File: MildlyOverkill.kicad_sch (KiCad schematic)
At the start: 68 parts, among them J1 USB_C_Receptacle_USB2.0_16P, J2 2604-1102, J3 2604-1104, J4 2604-1104, J5 Conn_01x04_Pin, J6 Conn_01x04_MountingPin, J7 Conn_01x04_Pin, Q5 QM6015D, U1 ESP32-S3-WROOM-1, U2 MCP3208, U3 LD1117S33TR_SOT223, U5 USBLC6-2P6, U6 TPS62932

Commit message: Added ethernet and ntcs
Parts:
- removed D24: 5V, LED_SMD:LED_0603_1608Metric, symbol Device:LED
- added C21, C36, C37, C38, C39, C40, C41: 0.1uF, symbol Device:C
- added C26, C35: 10uF 16V, symbol Device:C_Polarized
- added C27: 4.7uF, symbol Device:C
- added C28, C29, C30, C31: 10nF, symbol Device:C
- added C32: 22nF, symbol Device:C
- added C33, C34: 18pF, symbol Device:C
- added C42: 1nF 10kV, symbol Device:C
- added FB2: GZ2012D121TF, Inductor_THT:Choke_Schaffner_RN102-04-14.0x14.0mm, symbol Device:FerriteBead
- added J8: RJ45_Wuerth_7499010211A, Connector_RJ:RJ45_Wuerth_7499010211A_Horizontal, symbol Connector:RJ45_Wuerth_7499010211A
- added R41: 12.4K, Resistor_SMD:R_0805_2012Metric, symbol Device:R
- added R42, R43: 82, symbol Device:R
- added R44: 49, symbol Device:R
- added R66: 10, symbol Device:R
- added R73: 1M, symbol Device:R
- added R74: 0, symbol Device:R
- added R75, R76: 330, Resistor_SMD:R_0805_2012Metric, symbol Device:R
- added R77, R78, R79: R, symbol Device:R
- added TH1, TH2, TH3: Thermistor_NTC, Resistor_SMD:R_0805_2012Metric_Pad1.20x1.40mm_HandSolder, symbol Device:Thermistor_NTC
- added U7: W5500, Package_QFP:LQFP-48_7x7mm_P0.5mm, symbol Interface_Ethernet:W5500
- added Y1: 3134250001, Crystal:Crystal_SMD_3225-4Pin_3.2x2.5mm_HandSoldering, symbol Device:Crystal_GND24
- R62: value 210 -> 49; footprint Resistor_SMD:R_0805_2012Metric -> (none)
- R64, R65, R67, R68, R69, R70, R71, R72: footprint Resistor_SMD:R_0603_1608Metric_Pad0.98x0.95mm_HandSolder -> Resistor_SMD:R_0805_2012Metric_Pad1.20x1.40mm_HandSolder
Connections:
- net +3.3V: now also C21.1, C26.1, FB2.1, R77.1, R78.1, R79.1, U7.28 (VDD)
- net GND: now also D11.1 (K), D12.1 (K), D13.1 (K), D23.1 (K), C21.2, C26.2, C27.2, C28.2, C29.2, C32.1, C33.2, C34.2, C35.2, C36.2, C37.2, C38.2, C39.2, C40.2, C41.2, C42.1, J8.10, J8.11, R41.2, TH1.2, TH2.2, TH3.2, U7.14 (AGND), U7.16 (AGND), U7.19 (AGND), U7.29 (GND), U7.3 (AGND), U7.48 (AGND), U7.9 (AGND), Y1.2 (G), Y1.4 (G); no longer D11.2 (A), D12.2 (A), D13.2 (A), D23.2 (A)
- net MISO: now also U7.34 (MISO)
- net MOSI: now also U7.35 (MOSI)
- net SCLK: now also U7.33 (SCLK)
- net NTC1: now reaches U2.5 (CH4)
- net NTC1: now also R77.2, TH1.1
- net NTC2: now reaches U2.6 (CH5)
- net NTC2: now also R78.2, TH2.1
- net NTC3: now reaches U2.7 (CH6)
- net NTC3: now also R79.2, TH3.1
- net at R53.2: now also D12.2 (A); no longer D12.1 (K)
- net at R52.2: now also D11.2 (A); no longer D11.1 (K)
- net at R61.2: now also D23.2 (A); no longer D23.1 (K)
- net at R54.2: now also D13.2 (A); no longer D13.1 (K)
- net at R62.2: now also J8.2 (TD-), U7.1 (TXN)
- net LED2 renamed +3.3VA
- net +3.3VA: now also C35.1, C36.1, C37.1, C38.1, C39.1, C40.1, C41.1, FB2.2, R44.1, R66.1, U7.11 (AVDD), U7.15 (AVDD), U7.17 (AVDD), U7.21 (AVDD), U7.4 (AVDD), U7.8 (AVDD); no longer U1.31 (IO38)
- new net: C30.1, R43.1, U7.5 (RXN)
- new net: C30.2, J8.6 (RD-)
- new net: C32.2, J8.4 (CTD), R66.2
- new net: C28.1, U7.22 (1V2O)
- new net: J8.1 (TD+), R44.2, U7.2 (TXP)
- new net: R73.1, R74.2, U7.31 (XO)
- new net: C34.1, R73.2, U7.30 (XI/CLKIN), Y1.3
- new net: J8.9, R76.2
- new net: R41.1, U7.10 (EXRES1)
- new net: C27.1, U7.20 (TOCAP)
- new net: C31.1, R42.1, U7.6 (RXP)
- new net: C29.1, J8.5 (CRD), R42.2, R43.2
- new net: C33.1, R74.1, Y1.1
- new net: C42.2, J8.8, J8.SH
- new net: J8.12, R75.2
- new net: C31.2, J8.3 (RD+)
- new net ACT_LED: R76.1, U7.27 (ACTLED)
- new net ETH_CS: U1.31 (IO38), U7.32 (~{SCS})
- new net LINK_LED: R75.1, U7.25 (LINKLED)
- no-connect marks 7 -> 20
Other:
- note added: "Bussystems"
- note added: "NTCs"
- note added: "STEMMA QT (UwU)"
- note added: "USB"
- note removed: "Bussystems (i might add ethernet later on)"
- moved on the sheet: BOOT1, C1, C10, C11, C12, C13, C14, C16, C17, C2, C3, C4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

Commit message: kinda finished high power i guess
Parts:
- added H1, H2, H3, H4: MountingHole, MountingHole:MountingHole_2.1mm, symbol Mechanical:MountingHole
- added M1: Fan_4pin, Connector:FanPinHeader_1x04_P2.54mm_Vertical, symbol Motor:Fan_4pin
- C21, C36, C37, C38, C39, C40, C41: footprint (none) -> Capacitor_SMD:C_0603_1608Metric
- C26, C35: footprint (none) -> Capacitor_THT:CP_Radial_D4.0mm_P2.00mm
- C27: footprint (none) -> Capacitor_SMD:C_1206_3216Metric
- C28, C29, C30, C31, C32, C33, C34, C42: footprint (none) -> Capacitor_SMD:C_0805_2012Metric
- FB2: footprint Inductor_THT:Choke_Schaffner_RN102-04-14.0x14.0mm -> Inductor_SMD:L_0805_2012Metric
- J7: value Conn_01x04_Pin -> Conn_01x02_Pin; footprint Connector_PinHeader_2.54mm:PinHeader_1x04_P2.54mm_Vertical -> Connector_PinHeader_2.54mm:PinHeader_1x02_P2.54mm_Vertical; symbol Connector:Conn_01x04_Pin -> Connector:Conn_01x02_Pin
- R42, R43, R44, R62, R66, R73, R77, R78, R79: footprint (none) -> Resistor_SMD:R_0805_2012Metric
- R74: footprint (none) -> Capacitor_SMD:C_0603_1608Metric_Pad1.08x0.95mm_HandSolder
- TH2: footprint Resistor_SMD:R_0805_2012Metric_Pad1.20x1.40mm_HandSolder -> Connector_PinHeader_2.54mm:PinHeader_1x02_P2.54mm_Vertical
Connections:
- net +5V: now also M1.2 (+)
- net GND: now also M1.1 (-)
- net at U1.16 (IO46): now also M1.4 (PWM); no longer J7.3 (Pin_3)
- net at U1.26 (IO45): now also M1.3 (Tacho); no longer J7.4 (Pin_4)

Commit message: routed ethernet
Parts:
- C42: footprint Capacitor_SMD:C_0805_2012Metric -> Capacitor_SMD:C_1206_3216Metric
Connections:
- net shield: now reaches C42.2, J8.8, J8.SH
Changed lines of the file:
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@@
 		)
 	)
+	(label "shield"
+		(at 383.54 214.63 90)
+		(effects
+			(font
+				(size 1.27 1.27)
+			)
+			(justify left bottom)
+		)
+	)
 	(global_label "ST"
 		(shape input)
@@
 			)
 		)
-		(property "Footprint" "Capacitor_SMD:C_0805_2012Metric"
+		(property "Footprint" "Capacitor_SMD:C_1206_3216Metric"
 			(at 378.46 214.9348 0)
 			(hide yes)

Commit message: New refactor into a Smaler formfactor (2 Layer Possible?)
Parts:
- removed C17: 100nF, Capacitor_SMD:C_0603_1608Metric, symbol Device:C
- removed D9: 10V, Diode_SMD:D_SOD-123, symbol Device:D_Zener
- removed J2: 2604-1102, wago1102:CONN2_2604-1102_WAG, symbol 2026-09-05_10-49-54:2604-1102
- removed J3, J4: 2604-1104, wago1104:CONN4_2604-1104_WAG, symbol 2026-09-06_10-53-27:2604-1104
- removed J7: Conn_01x02_Pin, Connector_PinHeader_2.54mm:PinHeader_1x02_P2.54mm_Vertical, symbol Connector:Conn_01x02_Pin
- removed JP2, JP6, JP7, JP9: SolderJumper_3_Open, Jumper:SolderJumper-3_P2.0mm_Open_TrianglePad1.0x1.5mm_NumberLabels, symbol Jumper:SolderJumper_3_Open
- removed Q5: QM6015D, Package_TO_SOT_SMD:TO-252-2, symbol Transistor_FET:QM6015D
- removed R4: 10K, Resistor_SMD:R_0805_2012Metric, symbol Device:R
- removed R65, R69, R70, R72: R, Resistor_SMD:R_0805_2012Metric_Pad1.20x1.40mm_HandSolder, symbol Device:R
- removed R78, R79: R, Resistor_SMD:R_0805_2012Metric, symbol Device:R
- removed TH2: Thermistor_NTC, Connector_PinHeader_2.54mm:PinHeader_1x02_P2.54mm_Vertical, symbol Device:Thermistor_NTC
- removed TH3: Thermistor_NTC, Resistor_SMD:R_0805_2012Metric_Pad1.20x1.40mm_HandSolder, symbol Device:Thermistor_NTC
- added J2: Screw_Terminal_01x02, Connector_Phoenix_MSTB:PhoenixContact_MSTBA_2,5_2-G_1x02_P5.00mm_Horizontal, symbol Connector:Screw_Terminal_01x02
- added J3: Motors, TerminalBlock_Phoenix:TerminalBlock_Phoenix_MPT-0,5-4-2.54_1x04_P2.54mm_Horizontal, symbol Connector:Screw_Terminal_01x04
- added J4: IO, TerminalBlock_Phoenix:TerminalBlock_Phoenix_MPT-0,5-4-2.54_1x04_P2.54mm_Horizontal, symbol Connector:Screw_Terminal_01x04
- added J9: Analog, TerminalBlock_Phoenix:TerminalBlock_Phoenix_MPT-0,5-4-2.54_1x04_P2.54mm_Horizontal, symbol Connector:Screw_Terminal_01x04
- added R12, R14, R16, R18: 10k, Resistor_SMD:R_0805_2012Metric, symbol Device:R
- added R13, R15, R17, R19: 1k, Resistor_SMD:R_0805_2012Metric, symbol Device:R
- D11: value VSS -> LED
- D12: value 3.3V -> LED
- D13, D23: value 5V -> LED
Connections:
- net GND: now also J2.1 (Pin_1), R13.2, R15.2, R17.2, R19.2
- net IO1: now also J4.1 (Pin_1)
- net IO2: now also J4.2 (Pin_2)
- net IO3: now also J4.3 (Pin_3)
- net IO4: now also J4.4 (Pin_4)
- net RST: now also U7.37 (~{RST})
- net VCC: now also J2.2 (Pin_2)
- net EN1: no longer names the net of U1.19 (IO11)
- net EN2: no longer names the net of U1.20 (IO12)
- net EN3: no longer names the net of U1.21 (IO13)
- net EN4: no longer names the net of U1.22 (IO14)
- net GPIO1 renamed IN1.1
- net GPIO2 renamed IN1.2
- net GPIO3 renamed IN2.1
- net GPIO4 renamed IN2.2
- net IS1 renamed AIN1
- net AIN1: now also R12.2, R13.1
- net IS2 renamed AIN2
- net AIN2: now also R14.2, R15.1
- net IS3 renamed AIN3
- net AIN3: now also R16.2, R17.1
- net IS4 renamed AIN4
- net AIN4: now also R18.2, R19.1
- net NTC2 renamed CURR1
- net NTC3 renamed CURR2
- new net: J9.1 (Pin_1), R12.1
- new net: J9.2 (Pin_2), R14.1
- new net: J9.3 (Pin_3), R16.1
- new net: J9.4 (Pin_4), R18.1
- new net M1.1: J3.1 (Pin_1)
- new net M1.2: J3.2 (Pin_2)
- new net M2.1: J3.4 (Pin_4)
- new net M2.2: J3.3 (Pin_3)
- no-connect marks 20 -> 26
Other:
- removed sheet Power IO
- removed sheet Power IO1
- removed sheet Power IO2
- removed sheet Power IO3
- added sheet H-Bridge (H-Bridge.kicad_sch)
- added sheet H-Bridge1 (H-Bridge.kicad_sch)
- note added: "H bridges"
- note added: "NTC"
- note removed: "NTCs"
- note removed: "big H bridges"
- moved on the sheet: C16, C21, C26

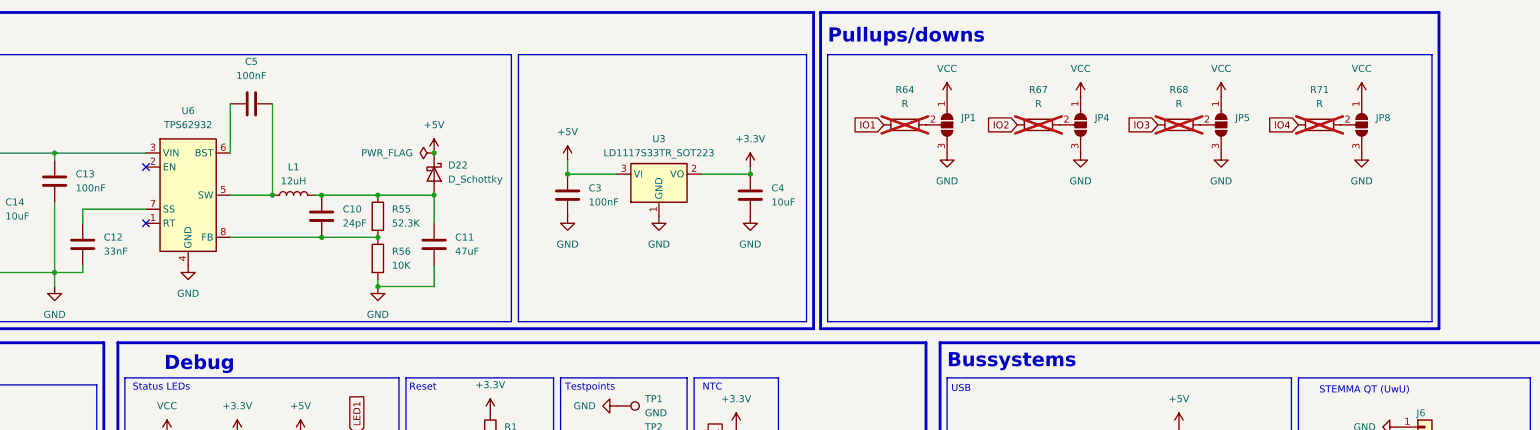
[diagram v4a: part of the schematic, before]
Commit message: Added custom footprint and made Buck samller
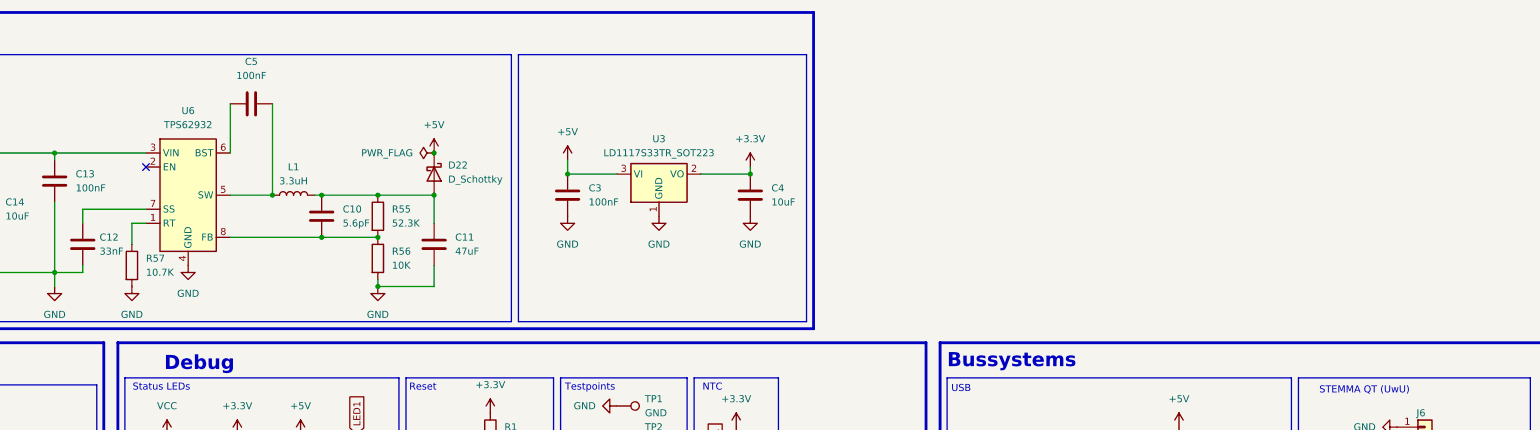
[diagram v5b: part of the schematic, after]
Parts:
- removed JP1, JP4, JP5, JP8: SolderJumper_3_Open, Jumper:SolderJumper-3_P2.0mm_Open_TrianglePad1.0x1.5mm_NumberLabels, symbol Jumper:SolderJumper_3_Open
- removed R64, R67, R68, R71: R, Resistor_SMD:R_0805_2012Metric_Pad1.20x1.40mm_HandSolder, symbol Device:R
- added R57: 10.7K, Resistor_SMD:R_0805_2012Metric, symbol Device:R
- C10: value 24pF -> 5.6pF
- L1: value 12uH -> 3.3uH; footprint Inductor_SMD:L_Bourns_SRR1208_12.7x12.7mm -> Library:WE-XHMI 4.3x4.3
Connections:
- net GND: now also R57.2
- net at U6.1 (RT): now also R57.1
- no-connect marks 26 -> 25
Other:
- note removed: "Pullups/downs"

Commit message: H-Bridges are done i guess
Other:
- moved on the sheet: C10, C11, C12, C13, C14, C16, C3, C4, C5, D22, J2, L1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

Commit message: Power stage almost done
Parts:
- added C17: 10uF, Capacitor_SMD:C_0603_1608Metric, symbol Device:C
- added D3: BZT52C15, Diode_SMD:D_0805_2012Metric, symbol Device:D_Zener
- added D4: SMAJ33A, Diode_SMD:D_SMA, symbol Diode:SMAJ33A
- added F1: Fuse, Fuse:Fuseholder_Blade_Mini_Keystone_3568, symbol Device:Fuse
- added Q1: Q_PMOS_GDS, Package_TO_SOT_SMD:TO-252-2, symbol Transistor_FET:Q_PMOS_GDS
- added R4: 100, Resistor_SMD:R_0805_2012Metric, symbol Device:R
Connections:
- net +5V: now also C10.2, R55.1, C17.2
- net GND: now also C17.1, D4.2 (A2), R4.1
- net VCC: now also D3.1 (K), Q1.3 (S); no longer J2.2 (Pin_2)
- net at C11.2, D22.2 (A), L1.2: no longer C10.2, R55.1
- new net: D4.1 (A1), F1.2, Q1.2 (D)
- new net: F1.1, J2.2 (Pin_2)
- new net: D3.2 (A), Q1.1 (G), R4.2
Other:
- moved on the sheet: C10, C11, C12, C13, C14, C16, C5, D22, J2, L1, R55, R56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

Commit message: Insane amounts of routing and Ethernet ist basicaly done.
DRC is going to be fun for future me...
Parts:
- added R64, R65, R67, R68: 33, Resistor_SMD:R_0603_1608Metric, symbol Device:R
- C29, C30, C31, C32: footprint Capacitor_SMD:C_0805_2012Metric -> Capacitor_SMD:C_0603_1608Metric
- R42, R43, R44, R62, R66: footprint Resistor_SMD:R_0805_2012Metric -> Resistor_SMD:R_0603_1608Metric
- R74: footprint Capacitor_SMD:C_0603_1608Metric_Pad1.08x0.95mm_HandSolder -> Resistor_SMD:R_0805_2012Metric_Pad1.20x1.40mm_HandSolder
- Y1: footprint Crystal:Crystal_SMD_3225-4Pin_3.2x2.5mm_HandSoldering -> Crystal:Crystal_SMD_3225-4Pin_3.2x2.5mm
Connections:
- net ETH_RX_B_N: now reaches C30.1, R43.1
- net ETH_RX_B_N: now also R67.2; no longer U7.5 (RXN)
- net ETH_RX_C_N: now reaches C30.2, J8.6 (RD-)
- net ETH_TX_B_P: now reaches J8.1 (TD+), R44.2
- net ETH_TX_B_P: now also R65.2; no longer U7.2 (TXP)
- net ETH_TX_B_N: now reaches J8.2 (TD-), R62.2
- net ETH_TX_B_N: now also R64.2; no longer U7.1 (TXN)
- net ETH_RX_B_P: now reaches C31.1, R42.1
- net ETH_RX_B_P: now also R68.2; no longer U7.6 (RXP)
- net ETH_RX_C_P: now reaches C31.2, J8.3 (RD+)
- new net ETH_RX_A_N: R67.1, U7.5 (RXN)
- new net ETH_RX_A_P: R68.1, U7.6 (RXP)
- new net ETH_TX_A_N: R64.1, U7.1 (TXN)
- new net ETH_TX_A_P: R65.1, U7.2 (TXP)
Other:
- moved on the sheet: C29, C30, C31, R42, R43
